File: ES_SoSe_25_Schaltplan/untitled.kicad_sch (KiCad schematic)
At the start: 9 parts, among them M1 Motor_DC, M2 Motor_Servo, U6 L298N

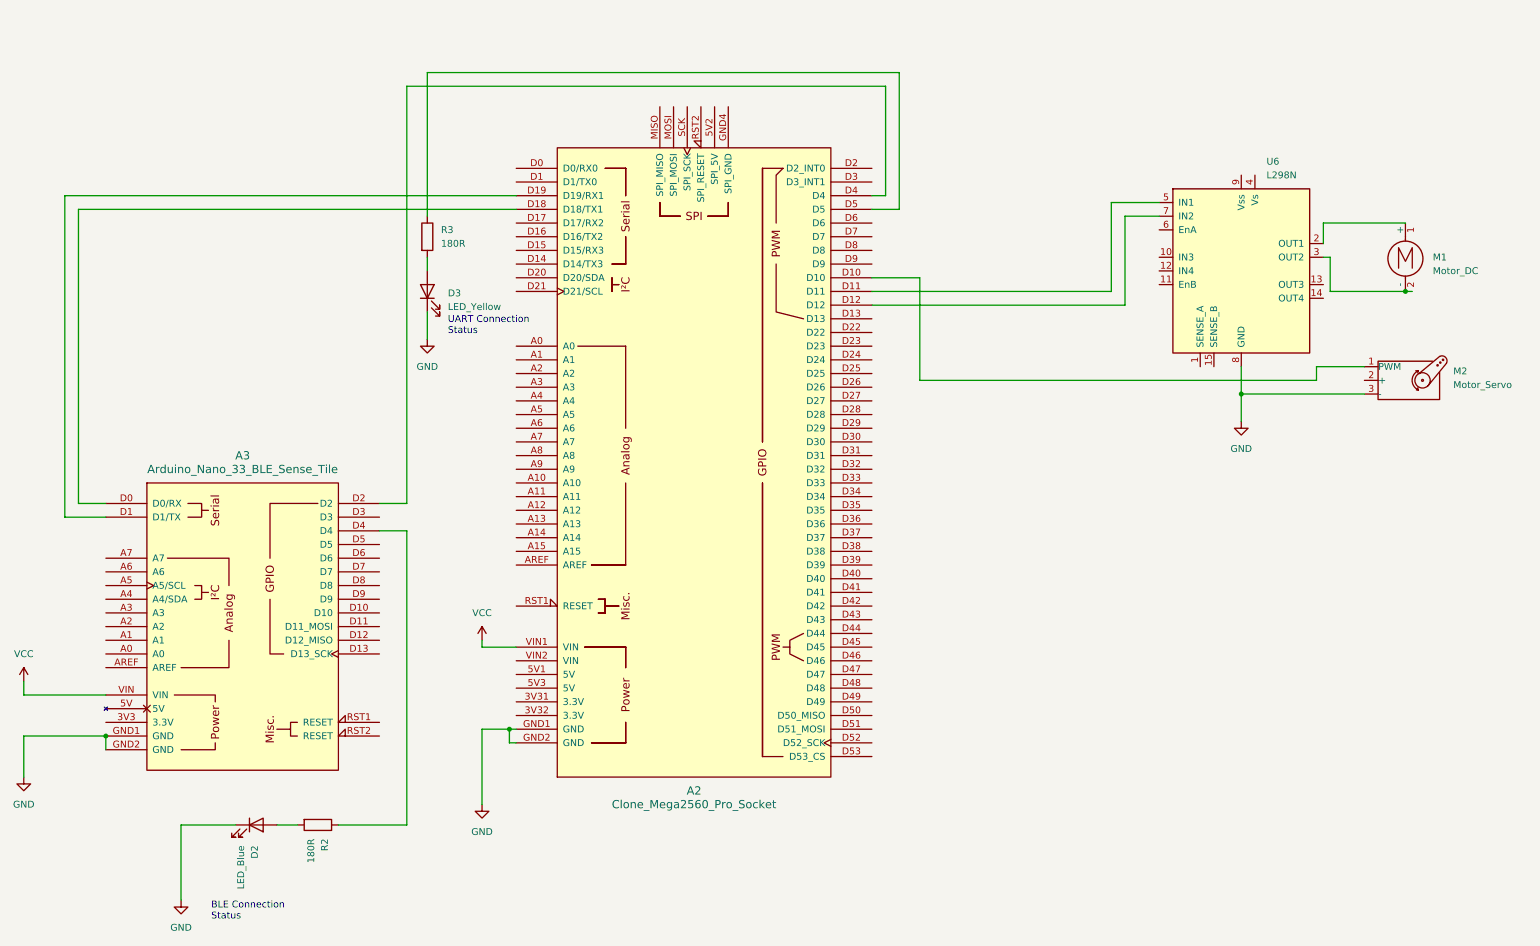
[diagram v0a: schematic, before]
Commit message: Schaltplan_änderung
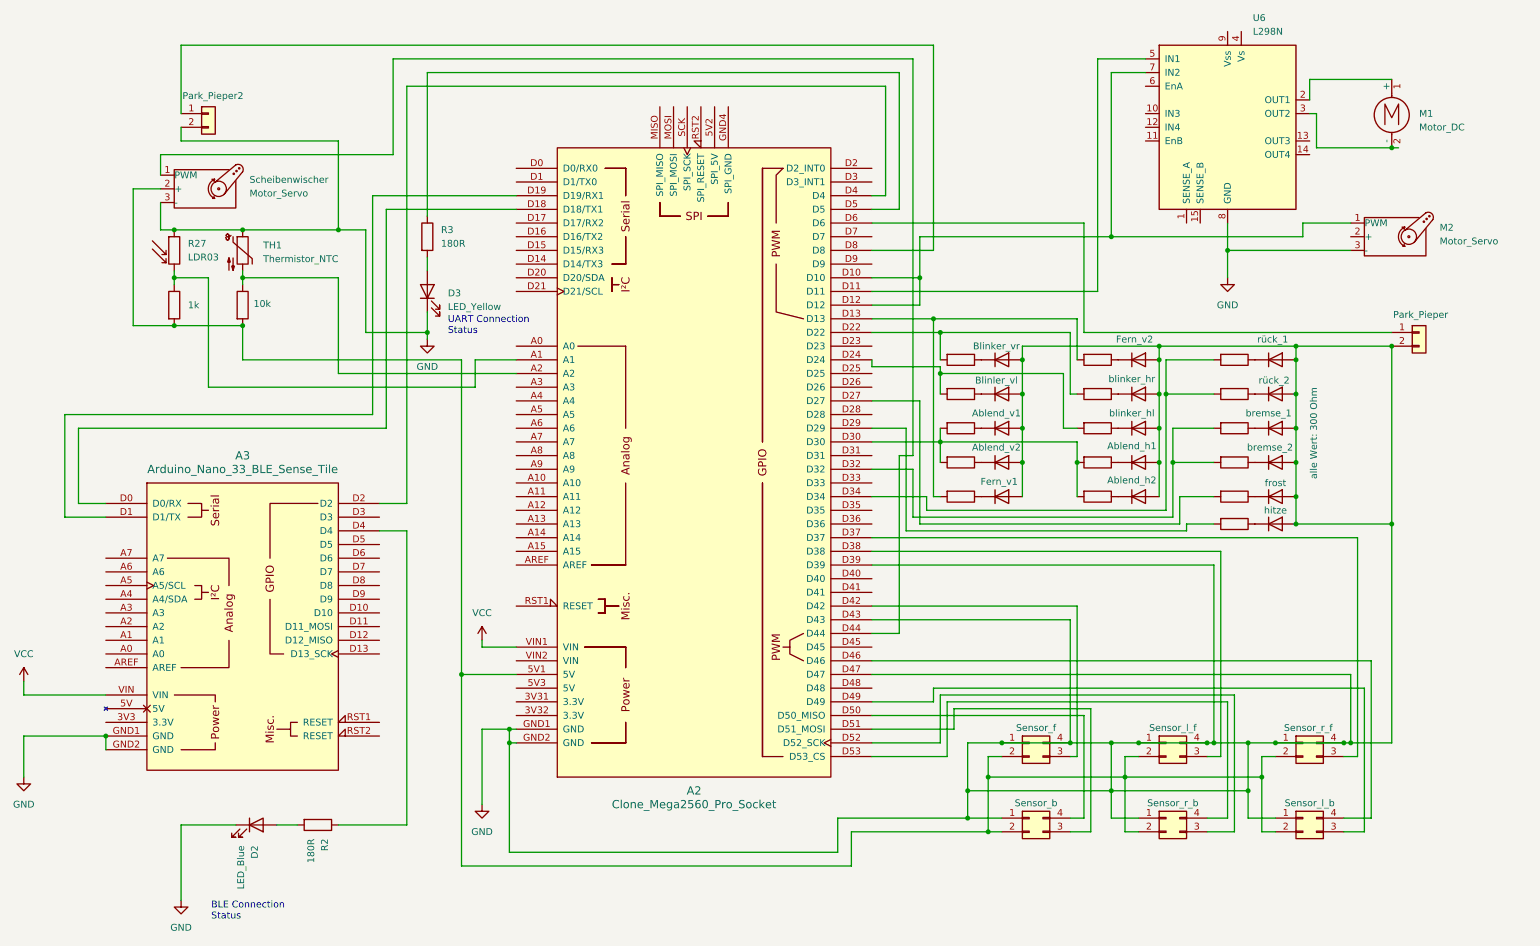
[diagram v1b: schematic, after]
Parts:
- added Ablend_h1, Ablend_h2, Ablend_v1, Ablend_v2, Blinker_vr, Blinler_vl, Fern_v1, Fern_v2, blinker_hl, blinker_hr, bremse_1, bremse_2, frost, hitze, rück_1, rück_2: 1N4148WT, Diode_SMD:D_SOD-523, symbol Diode:1N4148WT
- added Park_Pieper, Park_Pieper2: Conn_01x02, symbol Connector_Generic:Conn_01x02
- added R10, R11, R12, R13, R14, R15, R16, R17, R18, R19, R20, R22, R23, R24, R25: 180R, symbol Device:R
- added R21: alle Wert: 300 Ohm, symbol Device:R
- added R26: 10k, symbol Device:R
- added R27: LDR03, OptoDevice:R_LDR_10x8.5mm_P7.6mm_Vertical, symbol Sensor_Optical:LDR03
- added R28: 1k, symbol Device:R
- added Scheibenwischer: Motor_Servo, symbol Motor:Motor_Servo
- added Sensor_b, Sensor_f, Sensor_l_b, Sensor_l_f, Sensor_r_b, Sensor_r_f: Conn_02x02_Counter_Clockwise, symbol Connector_Generic:Conn_02x02_Counter_Clockwise
- added TH1: Thermistor_NTC, symbol Device:Thermistor_NTC
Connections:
- net GND: now also A2.D39, A2.D43, A2.D47, Ablend_h1.2 (A), Ablend_h2.2 (A), Ablend_v1.2 (A), Ablend_v2.2 (A), Blinker_vr.2 (A), Blinler_vl.2 (A), Fern_v1.2 (A), Fern_v2.2 (A), Park_Pieper.2 (Pin_2), Park_Pieper2.2 (Pin_2), R27.1, Scheibenwischer.3 (-), Sensor_b.1 (Pin_1), Sensor_f.1 (Pin_1), Sensor_f.4 (Pin_4), Sensor_l_b.1 (Pin_1), Sensor_l_f.1 (Pin_1), Sensor_l_f.4 (Pin_4), Sensor_r_b.1 (Pin_1), Sensor_r_f.1 (Pin_1), Sensor_r_f.4 (Pin_4), TH1.1, blinker_hl.2 (A), blinker_hr.2 (A), bremse_1.2 (A), bremse_2.2 (A), frost.2 (A), hitze.2 (A), rück_1.2 (A), rück_2.2 (A)
- net at A2.5V1 (5V): now also R26.2, R28.2, Scheibenwischer.2 (+), Sensor_b.2 (Pin_2), Sensor_f.2 (Pin_2), Sensor_l_b.2 (Pin_2), Sensor_l_f.2 (Pin_2), Sensor_r_b.2 (Pin_2), Sensor_r_f.2 (Pin_2)
- net at A2.A1: now also R27.2, R28.1
- net at A2.A2: now also R26.1, TH1.2
- net at A2.D10, M2.1 (PWM): now also A2.D12, U6.7 (IN2)
- net at A2.D13: now also R14.2, R15.2
- net at A2.D22: now also R10.2, R16.2
- net at A2.D24: now also R11.2, R17.2
- net at A2.D27: now also R24.2
- net at A2.D29: now also R25.2
- net at A2.D30: now also R12.2, R13.2, R18.2, R19.2
- net at A2.D32: now also R22.2, R23.2
- net at A2.D34: now also R20.2, R21.2
- net at A2.D37: now also Sensor_r_f.3 (Pin_3)
- net at A2.D38: now also Sensor_l_f.3 (Pin_3)
- net at A2.D42: now also Sensor_f.3 (Pin_3)
- net at A2.D44: now also Scheibenwischer.1 (PWM)
- net at A2.D46: now also Sensor_l_b.4 (Pin_4)
- net at A2.D49: now also Sensor_l_b.3 (Pin_3)
- net at A2.D50 (D50_MISO): now also Sensor_b.4 (Pin_4)
- net at A2.D51 (D51_MOSI): now also Sensor_b.3 (Pin_3)
- net at A2.D52 (D52_SCK): now also Sensor_r_b.3 (Pin_3)
- net at A2.D53 (D53_CS): now also Sensor_r_b.4 (Pin_4)
- net at A2.D6: now also Park_Pieper.1 (Pin_1)
- net at A2.D8: now also Park_Pieper2.1 (Pin_1)
- new net: Ablend_h1.1 (K), R18.1
- new net: R20.1, rück_1.1 (K)
- new net: R21.1, rück_2.1 (K)
- new net: Ablend_h2.1 (K), R19.1
- new net: R22.1, bremse_1.1 (K)
- new net: Ablend_v2.1 (K), R13.1
- new net: Ablend_v1.1 (K), R12.1
- new net: Blinker_vr.1 (K), R10.1
- new net: R23.1, bremse_2.1 (K)
- new net: R16.1, blinker_hr.1 (K)
- new net: Fern_v2.1 (K), R15.1
- new net: R24.1, frost.1 (K)
- new net: Fern_v1.1 (K), R14.1
- new net: Blinler_vl.1 (K), R11.1
- new net: R17.1, blinker_hl.1 (K)
- new net: R25.1, hitze.1 (K)
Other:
- moved on the sheet: M1, M2, U6
